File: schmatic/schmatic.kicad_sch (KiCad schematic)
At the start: 8 parts, among them J1 RFIO-RC522, J2 RTC, U1 LCD-016N002L

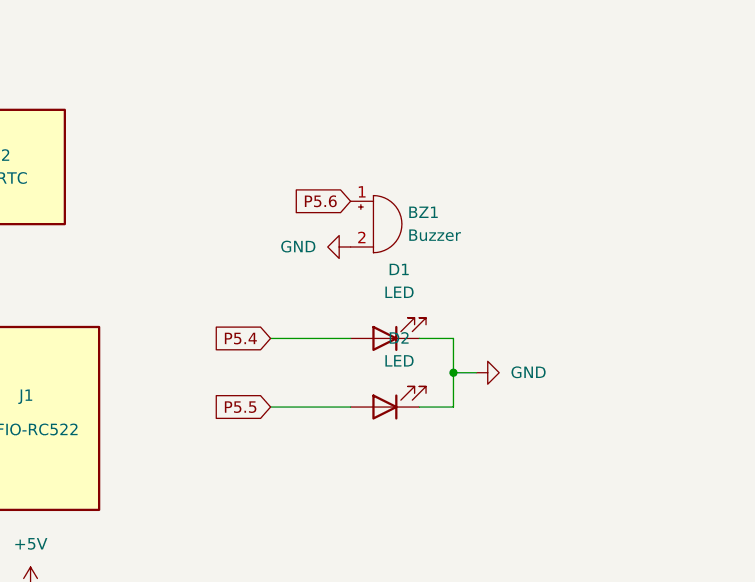
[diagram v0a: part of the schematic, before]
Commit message: fixed schmatic mistakes
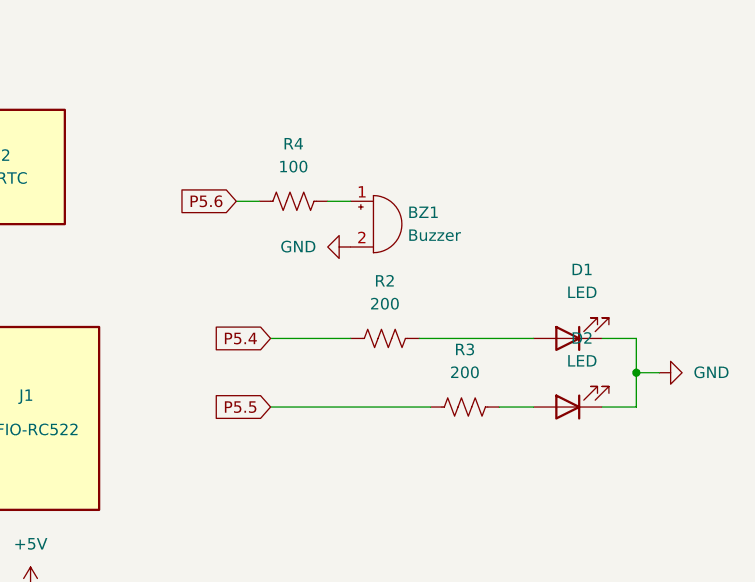
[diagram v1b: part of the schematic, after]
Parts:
- added R2, R3: 200, symbol Device:R_US
- added R4: 100, symbol Device:R_US
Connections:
- net P5.4: now also R2.1; no longer D1.2 (A)
- net P5.5: now also R3.2; no longer D2.2 (A)
- net P5.6: now also R4.2; no longer BZ1.1 (+)
- new net: D1.2 (A), R2.2
- new net: D2.2 (A), R3.1
- new net: BZ1.1 (+), R4.1
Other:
- moved on the sheet: D1, D2
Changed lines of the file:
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@@
   (junction (at 134.62 101.6) (diameter 0) (color 0 0 0 0)
   )
-  (junction (at 181.61 73.66) (diameter 0) (color 0 0 0 0)
+  (junction (at 201.93 73.66) (diameter 0) (color 0 0 0 0)
   )
   (junction (at 134.62 149.86) (diameter 0) (color 0 0 0 0)
@@
     (stroke (width 0) (type default))
   )
+  (wire (pts (xy 157.48 54.61) (xy 160.02 54.61))
+    (stroke (width 0) (type default))
+  )
   (wire (pts (xy 107.95 48.26) (xy 107.95 40.64))
     (stroke (width 0) (type default))
@@
     (stroke (width 0) (type default))
   )
-  (wire (pts (xy 181.61 69.85) (xy 181.61 73.66))
+  (wire (pts (xy 201.93 69.85) (xy 201.93 73.66))
     (stroke (width 0) (type default))
   )
@@
     (stroke (width 0) (type default))
   )
-  (wire (pts (xy 161.29 77.47) (xy 170.18 77.47))
-    (stroke (width 0) (type default))
-  )
   (wire (pts (xy 116.84 82.55) (xy 110.49 82.55))
     (stroke (width 0) (type default))
@@
     (stroke (width 0) (type default))
   )
+  (wire (pts (xy 167.64 54.61) (xy 170.18 54.61))
+    (stroke (width 0) (type default))
+  )
   (wire (pts (xy 144.78 121.92) (xy 156.21 121.92))
     (stroke (width 0) (type default))
@@
     (stroke (width 0) (type default))
   )
-  (wire (pts (xy 177.8 69.85) (xy 181.61 69.85))
+  (wire (pts (xy 198.12 69.85) (xy 201.93 69.85))
+    (stroke (width 0) (type default))
+  )
+  (wire (pts (xy 161.29 77.47) (xy 179.07 77.47))
     (stroke (width 0) (type default))
   )
@@
     (stroke (width 0) (type default))
   )
-  (wire (pts (xy 181.61 73.66) (xy 184.15 73.66))
+  (wire (pts (xy 201.93 73.66) (xy 204.47 73.66))
     (stroke (width 0) (type default))
   )
@@
     (stroke (width 0) (type default))
   )
+  (wire (pts (xy 177.8 69.85) (xy 190.5 69.85))
+    (stroke (width 0) (type default))
+  )
   (wire (pts (xy 111.76 80.01) (xy 116.84 80.01))
     (stroke (width 0) (type default))
@@
     (stroke (width 0) (type default))
   )
-  (wire (pts (xy 177.8 77.47) (xy 181.61 77.47))
+  (wire (pts (xy 198.12 77.47) (xy 201.93 77.47))
     (stroke (width 0) (type default))
   )
@@
     (stroke (width 0) (type default))
   )
+  (wire (pts (xy 110.49 85.09) (xy 116.84 85.09))
+    (stroke (width 0) (type default))
+  )
+  (wire (pts (xy 110.49 69.85) (xy 110.49 72.39))
+    (stroke (width 0) (type default))
+  )
+  (wire (pts (xy 111.76 53.34) (xy 111.76 54.61))
+    (stroke (width 0) (type default))
+  )
+  (wire (pts (xy 181.61 101.6) (xy 156.21 101.6))
+    (stroke (width 0) (type default))
+  )
+  (wire (pts (xy 201.93 77.47) (xy 201.93 73.66))
+    (stroke (width 0) (type default))
+  )
+  (wire (pts (xy 107.95 66.04) (xy 111.76 66.04))
+    (stroke (width 0) (type default))
+  )
+  (wire (pts (xy 107.95 69.85) (xy 110.49 69.85))
+    (stroke (width 0) (type default))
+  )
+  (wire (pts (xy 107.95 73.66) (xy 111.76 73.66))
+    (stroke (width 0) (type default))
+  )
+  (wire (pts (xy 186.69 77.47) (xy 190.5 77.47))
+    (stroke (width 0) (type default))
+  )
+  (wire (pts (xy 110.49 82.55) (xy 110.49 85.09))
+    (stroke (width 0) (type default))
+  )
   (wire (pts (xy 161.29 69.85) (xy 170.18 69.85))
     (stroke (width 0) (type default))
   )
-  (wire (pts (xy 110.49 85.09) (xy 116.84 85.09))
-    (stroke (width 0) (type default))
-  )
-  (wire (pts (xy 110.49 69.85) (xy 110.49 72.39))
-    (stroke (width 0) (type default))
-  )
-  (wire (pts (xy 111.76 53.34) (xy 111.76 54.61))
-    (stroke (width 0) (type default))
-  )
-  (wire (pts (xy 181.61 101.6) (xy 156.21 101.6))
-    (stroke (width 0) (type default))
-  )
-  (wire (pts (xy 181.61 77.47) (xy 181.61 73.66))
-    (stroke (width 0) (type default))
-  )
-  (wire (pts (xy 107.95 66.04) (xy 111.76 66.04))
-    (stroke (width 0) (type default))
-  )
-  (wire (pts (xy 107.95 69.85) (xy 110.49 69.85))
-    (stroke (width 0) (type default))
-  )
-  (wire (pts (xy 107.95 73.66) (xy 111.76 73.66))
-    (stroke (width 0) (type default))
-  )
-  (wire (pts (xy 110.49 82.55) (xy 110.49 85.09))
-    (stroke (width 0) (type default))
-  )
   (wire (pts (xy 116.84 48.26) (xy 107.95 48.26))
     (stroke (width 0) (type default))
@@
     )
   )
-  (global_label "P5.6" (shape input) (at 170.18 54.61 180) (fields_autoplaced)
-    (effects (font (size 1.27 1.27)) (justify right))
-    (property "Intersheetrefs" "${INTERSHEET_REFS}" (at 162.901 54.61 0)
+  (global_label "P5.6" (shape input) (at 157.48 54.61 180) (fields_autoplaced)
+    (effects (font (size 1.27 1.27)) (justify right))
+    (property "Intersheetrefs" "${INTERSHEET_REFS}" (at 150.201 54.61 0)
       (effects (font (size 1.27 1.27)) (justify right) hide)
     )
@@
     )
   )
-  (symbol (lib_id "Device:LED") (at 173.99 77.47 180) (unit 1)
-    (in_bom yes) (on_board yes) (dnp no) (fields_autoplaced)
-    (property "Reference" "D2" (at 175.5775 69.85 0)
-      (effects (font (size 1.27 1.27)))
-    )
-    (property "Value" "LED" (at 175.5775 72.39 0)
-      (effects (font (size 1.27 1.27)))
-    )
-    (property "Footprint" "" (at 173.99 77.47 0)
-      (effects (font (size 1.27 1.27)) hide)
-    )
-    (property "Datasheet" "~" (at 173.99 77.47 0)
+  (symbol (lib_id "Device:R_US") (at 173.99 69.85 90) (unit 1)
+    (in_bom yes) (on_board yes) (dnp no) (fields_autoplaced)
+    (property "Reference" "R2" (at 173.99 63.5 90)
+      (effects (font (size 1.27 1.27)))
+    )
+    (property "Value" "200" (at 173.99 66.04 90)
+      (effects (font (size 1.27 1.27)))
+    )
+    (property "Footprint" "" (at 174.244 68.834 90)
+      (effects (font (size 1.27 1.27)) hide)
+    )
+    (property "Datasheet" "~" (at 173.99 69.85 0)
+      (effects (font (size 1.27 1.27)) hide)
+    )
+    (pin "1")
+    (pin "2")
+    (instances
+      (project "schmatic"
+        (path "/4d91ea9c-4d21-4759-83b5-41660ef12129"
+          (reference "R2") (unit 1)
+        )
+      )
+    )
+  )
+  (symbol (lib_id "Device:LED") (at 194.31 77.47 180) (unit 1)
+    (in_bom yes) (on_board yes) (dnp no) (fields_autoplaced)
+    (property "Reference" "D2" (at 195.8975 69.85 0)
+      (effects (font (size 1.27 1.27)))
+    )
+    (property "Value" "LED" (at 195.8975 72.39 0)
+      (effects (font (size 1.27 1.27)))
+    )
+    (property "Footprint" "" (at 194.31 77.47 0)
+      (effects (font (size 1.27 1.27)) hide)
+    )
+    (property "Datasheet" "~" (at 194.31 77.47 0)
       (effects (font (size 1.27 1.27)) hide)
     )
@@
     )
   )
-  (symbol (lib_id "power:GND") (at 184.15 73.66 90) (unit 1)
-    (in_bom yes) (on_board yes) (dnp no) (fields_autoplaced)
-    (property "Reference" "#PWR08" (at 190.5 73.66 0)
-      (effects (font (size 1.27 1.27)) hide)
-    )
-    (property "Value" "GND" (at 187.96 73.66 90)
+  (symbol (lib_id "Device:R_US") (at 163.83 54.61 270) (unit 1)
+    (in_bom yes) (on_board yes) (dnp no) (fields_autoplaced)
+    (property "Reference" "R4" (at 163.83 48.26 90)
+      (effects (font (size 1.27 1.27)))
+    )
+    (property "Value" "100" (at 163.83 50.8 90)
+      (effects (font (size 1.27 1.27)))
+    )
+    (property "Footprint" "" (at 163.576 55.626 90)
+      (effects (font (size 1.27 1.27)) hide)
+    )
+    (property "Datasheet" "~" (at 163.83 54.61 0)
+      (effects (font (size 1.27 1.27)) hide)
+    )
+    (pin "1")
+    (pin "2")
+    (instances
+      (project "schmatic"
+        (path "/4d91ea9c-4d21-4759-83b5-41660ef12129"
+          (reference "R4") (unit 1)
+        )
+      )
+    )
+  )
+  (symbol (lib_id "Device:R_US") (at 182.88 77.47 270) (unit 1)
+    (in_bom yes) (on_board yes) (dnp no) (fields_autoplaced)
+    (property "Reference" "R3" (at 182.88 71.12 90)
+      (effects (font (size 1.27 1.27)))
+    )
+    (property "Value" "200" (at 182.88 73.66 90)
+      (effects (font (size 1.27 1.27)))
+    )
+    (property "Footprint" "" (at 182.626 78.486 90)
+      (effects (font (size 1.27 1.27)) hide)
+    )
+    (property "Datasheet" "~" (at 182.88 77.47 0)
+      (effects (font (size 1.27 1.27)) hide)
+    )
+    (pin "2")
+    (pin "1")
+    (instances
+      (project "schmatic"
+        (path "/4d91ea9c-4d21-4759-83b5-41660ef12129"
+          (reference "R3") (unit 1)
+        )
+      )
+    )
+  )
+  (symbol (lib_id "power:GND") (at 204.47 73.66 90) (unit 1)
+    (in_bom yes) (on_board yes) (dnp no) (fields_autoplaced)
+    (property "Reference" "#PWR08" (at 210.82 73.66 0)
+      (effects (font (size 1.27 1.27)) hide)
+    )
+    (property "Value" "GND" (at 208.28 73.66 90)
       (effects (font (size 1.27 1.27)) (justify right))
     )
-    (property "Footprint" "" (at 184.15 73.66 0)
-      (effects (font (size 1.27 1.27)) hide)
-    )
-    (property "Datasheet" "" (at 184.15 73.66 0)
+    (property "Footprint" "" (at 204.47 73.66 0)
+      (effects (font (size 1.27 1.27)) hide)
+    )
+    (property "Datasheet" "" (at 204.47 73.66 0)
       (effects (font (size 1.27 1.27)) hide)
     )
@@
     )
   )
-  (symbol (lib_id "Device:LED") (at 173.99 69.85 180) (unit 1)
-    (in_bom yes) (on_board yes) (dnp no) (fields_autoplaced)
-    (property "Reference" "D1" (at 175.5775 62.23 0)
-      (effects (font (size 1.27 1.27)))
-    )
-    (property "Value" "LED" (at 175.5775 64.77 0)
-      (effects (font (size 1.27 1.27)))
-    )
-    (property "Footprint" "" (at 173.99 69.85 0)
-      (effects (font (size 1.27 1.27)) hide)
-    )
-    (property "Datasheet" "~" (at 173.99 69.85 0)
-      (effects (font (size 1.27 1.27)) hide)
-    )
+  (symbol (lib_id "Device:LED") (at 194.31 69.85 180) (unit 1)
+    (in_bom yes) (on_board yes) (dnp no) (fields_autoplaced)
+    (property "Reference" "D1" (at 195.8975 62.23 0)
+      (effects (font (size 1.27 1.27)))
+    )
+    (property "Value" "LED" (at 195.8975 64.77 0)
+      (effects (font (size 1.27 1.27)))
+    )
+    (property "Footprint" "" (at 194.31 69.85 0)
+      (effects (font (size 1.27 1.27)) hide)
+    )
+    (property "Datasheet" "~" (at 194.31 69.85 0)
+      (effects (font (size 1.27 1.27)) hide)
+    )

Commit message: updated schmatic
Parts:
- removed R4: 100, symbol Device:R_US
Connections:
- net +3.3V: no longer J2.2 (VCC)
- net +5V: now also J2.2 (VCC)
- net P5.6: now also BZ1.1 (+)
- net P3.0: no longer names the net of J1.5 (RQ)
- net P5.4 renamed P2.4
- net P5.5 renamed P2.3
- no-connect marks 1 -> 2
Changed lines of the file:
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@@
   )
   (no_connect (at 114.3 55.88))
+  (no_connect (at 116.84 80.01))
   (wire (pts (xy 116.84 129.54) (xy 124.46 129.54))
     (stroke (width 0) (type default))
@@
     (stroke (width 0) (type default))
   )
-  (wire (pts (xy 157.48 54.61) (xy 160.02 54.61))
+  (wire (pts (xy 166.37 54.61) (xy 170.18 54.61))
     (stroke (width 0) (type default))
   )
@@
     (stroke (width 0) (type default))
   )
+  (wire (pts (xy 166.37 59.69) (xy 170.18 59.69))
+    (stroke (width 0) (type default))
+  )
   (wire (pts (xy 115.57 110.49) (xy 120.65 110.49))
     (stroke (width 0) (type default))
@@
     (stroke (width 0) (type default))
   )
-  (wire (pts (xy 107.95 81.28) (xy 111.76 81.28))
-    (stroke (width 0) (type default))
-  )
   (wire (pts (xy 116.84 82.55) (xy 110.49 82.55))
     (stroke (width 0) (type default))
@@
     (stroke (width 0) (type default))
   )
-  (wire (pts (xy 167.64 54.61) (xy 170.18 54.61))
-    (stroke (width 0) (type default))
-  )
   (wire (pts (xy 144.78 121.92) (xy 156.21 121.92))
     (stroke (width 0) (type default))
@@
     (stroke (width 0) (type default))
   )
-  (wire (pts (xy 111.76 80.01) (xy 116.84 80.01))
-    (stroke (width 0) (type default))
-  )
   (wire (pts (xy 105.41 101.6) (xy 134.62 101.6))
     (stroke (width 0) (type default))
@@
     (stroke (width 0) (type default))
   )
-  (wire (pts (xy 111.76 81.28) (xy 111.76 80.01))
-    (stroke (width 0) (type default))
-  )
   (wire (pts (xy 120.65 111.76) (xy 124.46 111.76))
     (stroke (width 0) (type default))
@@
     (stroke (width 0) (type default))
   )
-  (global_label "P5.5" (shape input) (at 161.29 77.47 180) (fields_autoplaced)
+  (global_label "P2.3" (shape input) (at 161.29 77.47 180) (fields_autoplaced)
     (effects (font (size 1.27 1.27)) (justify right))
     (property "Intersheetrefs" "${INTERSHEET_REFS}" (at 154.011 77.47 0)
@@
     )
   )
-  (global_label "P5.6" (shape input) (at 157.48 54.61 180) (fields_autoplaced)
-    (effects (font (size 1.27 1.27)) (justify right))
-    (property "Intersheetrefs" "${INTERSHEET_REFS}" (at 150.201 54.61 0)
+  (global_label "P5.6" (shape input) (at 166.37 54.61 180) (fields_autoplaced)
+    (effects (font (size 1.27 1.27)) (justify right))
+    (property "Intersheetrefs" "${INTERSHEET_REFS}" (at 159.091 54.61 0)
       (effects (font (size 1.27 1.27)) (justify right) hide)
     )
@@
     )
   )
-  (global_label "P5.4" (shape input) (at 161.29 69.85 180) (fields_autoplaced)
+  (global_label "P2.4" (shape input) (at 161.29 69.85 180) (fields_autoplaced)
     (effects (font (size 1.27 1.27)) (justify right))
     (property "Intersheetrefs" "${INTERSHEET_REFS}" (at 154.011 69.85 0)
@@
     (effects (font (size 1.27 1.27)) (justify right))
     (property "Intersheetrefs" "${INTERSHEET_REFS}" (at 100.671 50.8 0)
-      (effects (font (size 1.27 1.27)) (justify right) hide)
-    )
-  )
-  (global_label "P3.0" (shape input) (at 107.95 81.28 180) (fields_autoplaced)
-    (effects (font (size 1.27 1.27)) (justify right))
-    (property "Intersheetrefs" "${INTERSHEET_REFS}" (at 100.671 81.28 0)
       (effects (font (size 1.27 1.27)) (justify right) hide)
     )
@@
     )
   )
-  (symbol (lib_id "power:+3.3V") (at 107.95 40.64 0) (unit 1)
-    (in_bom yes) (on_board yes) (dnp no) (fields_autoplaced)
-    (property "Reference" "#PWR03" (at 107.95 44.45 0)
-      (effects (font (size 1.27 1.27)) hide)
-    )
-    (property "Value" "+3.3V" (at 107.95 35.56 0)
-      (effects (font (size 1.27 1.27)))
-    )
-    (property "Footprint" "" (at 107.95 40.64 0)
-      (effects (font (size 1.27 1.27)) hide)
-    )
-    (property "Datasheet" "" (at 107.95 40.64 0)
-      (effects (font (size 1.27 1.27)) hide)
-    )
-    (pin "1")
-    (instances
-      (project "schmatic"
-        (path "/4d91ea9c-4d21-4759-83b5-41660ef12129"
-          (reference "#PWR03") (unit 1)
-        )
-      )
-    )
-  )
   (symbol (lib_id "Device:R_US") (at 173.99 69.85 90) (unit 1)
     (in_bom yes) (on_board yes) (dnp no) (fields_autoplaced)
@@
     )
   )
-  (symbol (lib_id "Device:R_US") (at 163.83 54.61 270) (unit 1)
-    (in_bom yes) (on_board yes) (dnp no) (fields_autoplaced)
-    (property "Reference" "R4" (at 163.83 48.26 90)
-      (effects (font (size 1.27 1.27)))
-    )
-    (property "Value" "100" (at 163.83 50.8 90)
-      (effects (font (size 1.27 1.27)))
-    )
-    (property "Footprint" "" (at 163.576 55.626 90)
-      (effects (font (size 1.27 1.27)) hide)
-    )
-    (property "Datasheet" "~" (at 163.83 54.61 0)
-      (effects (font (size 1.27 1.27)) hide)
-    )
-    (pin "1")
-    (pin "2")
-    (instances
-      (project "schmatic"
-        (path "/4d91ea9c-4d21-4759-83b5-41660ef12129"
-          (reference "R4") (unit 1)
-        )
-      )
-    )
-  )
   (symbol (lib_id "Device:R_US") (at 182.88 77.47 270) (unit 1)
     (in_bom yes) (on_board yes) (dnp no) (fields_autoplaced)
@@
     )
   )
-  (symbol (lib_id "power:GND") (at 170.18 59.69 270) (unit 1)
-    (in_bom yes) (on_board yes) (dnp no) (fields_autoplaced)
-    (property "Reference" "#PWR07" (at 163.83 59.69 0)
-      (effects (font (size 1.27 1.27)) hide)
-    )
-    (property "Value" "GND" (at 166.37 59.69 90)
+  (symbol (lib_id "power:GND") (at 166.37 59.69 270) (unit 1)
+    (in_bom yes) (on_board yes) (dnp no) (fields_autoplaced)
+    (property "Reference" "#PWR07" (at 160.02 59.69 0)
+      (effects (font (size 1.27 1.27)) hide)
+    )
+    (property "Value" "GND" (at 162.56 59.69 90)
       (effects (font (size 1.27 1.27)) (justify right))
     )
-    (property "Footprint" "" (at 170.18 59.69 0)
-      (effects (font (size 1.27 1.27)) hide)
-    )
-    (property "Datasheet" "" (at 170.18 59.69 0)
+    (property "Footprint" "" (at 166.37 59.69 0)
+      (effects (font (size 1.27 1.27)) hide)
+    )
+    (property "Datasheet" "" (at 166.37 59.69 0)
       (effects (font (size 1.27 1.27)) hide)
     )
@@
         )
       )
+    )
+  )
+  (symbol (lib_id "power:+5V") (at 107.95 40.64 0) (unit 1)
+    (in_bom yes) (on_board yes) (dnp no) (fields_autoplaced)
+    (property "Reference" "#PWR03" (at 107.95 44.45 0)
+      (effects (font (size 1.27 1.27)) hide)
+    )
+    (property "Value" "+5V" (at 107.95 35.56 0)
+      (effects (font (size 1.27 1.27)))
+    )
+    (property "Footprint" "" (at 107.95 40.64 0)
+      (effects (font (size 1.27 1.27)) hide)
+    )
+    (property "Datasheet" "" (at 107.95 40.64 0)
+      (effects (font (size 1.27 1.27)) hide)
+    )
+    (pin "1")
+    (instances
+      (project "schmatic"
+        (path "/4d91ea9c-4d21-4759-83b5-41660ef12129"
+          (reference "#PWR03") (unit 1)
+        )
+      )

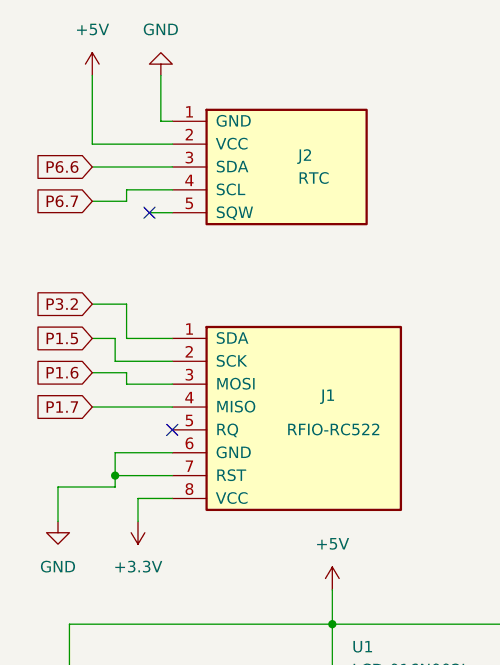
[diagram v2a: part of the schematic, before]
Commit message: flowchart updates and code cleanup
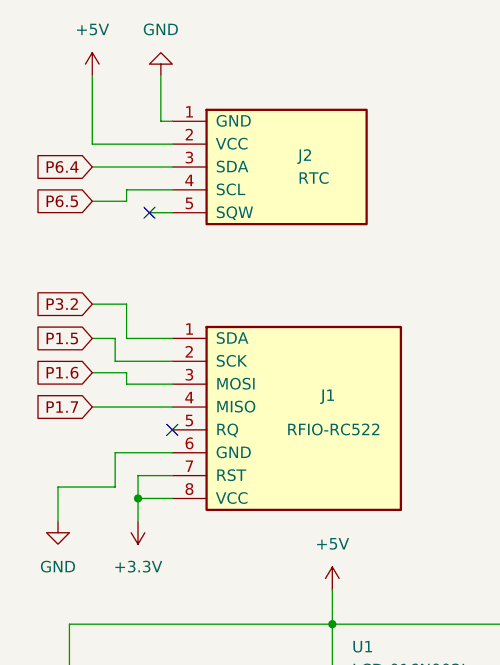
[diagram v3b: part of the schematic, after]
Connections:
- net +3.3V: now also J1.7 (RST)
- net GND: no longer J1.7 (RST)
- net P6.6 renamed P6.4
- net P6.7 renamed P6.5
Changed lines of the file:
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@@
 (kicad_sch (version 20230121) (generator eeschema)
   (paper "A")
-  (junction (at 110.49 85.09) (diameter 0) (color 0 0 0 0)
+  (junction (at 113.03 87.63) (diameter 0) (color 0 0 0 0)
   )
   (junction (at 156.21 121.92) (diameter 0) (color 0 0 0 0)
@@
     (stroke (width 0) (type default))
   )
+  (wire (pts (xy 116.84 85.09) (xy 113.03 85.09))
+    (stroke (width 0) (type default))
+  )
   (wire (pts (xy 111.76 54.61) (xy 107.95 54.61))
     (stroke (width 0) (type default))
@@
     (stroke (width 0) (type default))
   )
-  (wire (pts (xy 110.49 85.09) (xy 110.49 86.36))
+  (wire (pts (xy 110.49 82.55) (xy 110.49 86.36))
     (stroke (width 0) (type default))
   )
@@
     (stroke (width 0) (type default))
   )
+  (wire (pts (xy 113.03 85.09) (xy 113.03 87.63))
+    (stroke (width 0) (type default))
+  )
   (wire (pts (xy 134.62 149.86) (xy 156.21 149.86))
     (stroke (width 0) (type default))
@@
     (stroke (width 0) (type default))
   )
-  (wire (pts (xy 110.49 85.09) (xy 116.84 85.09))
-    (stroke (width 0) (type default))
-  )
   (wire (pts (xy 110.49 69.85) (xy 110.49 72.39))
     (stroke (width 0) (type default))
@@
     (stroke (width 0) (type default))
   )
-  (wire (pts (xy 110.49 82.55) (xy 110.49 85.09))
-    (stroke (width 0) (type default))
-  )
   (wire (pts (xy 161.29 69.85) (xy 170.18 69.85))
     (stroke (width 0) (type default))
@@
     )
   )
-  (global_label "P6.7" (shape input) (at 107.95 54.61 180) (fields_autoplaced)
+  (global_label "P6.5" (shape input) (at 107.95 54.61 180) (fields_autoplaced)
     (effects (font (size 1.27 1.27)) (justify right))
     (property "Intersheetrefs" "${INTERSHEET_REFS}" (at 100.671 54.61 0)
@@
     )
   )
-  (global_label "P6.6" (shape input) (at 107.95 50.8 180) (fields_autoplaced)
+  (global_label "P6.4" (shape input) (at 107.95 50.8 180) (fields_autoplaced)
     (effects (font (size 1.27 1.27)) (justify right))
     (property "Intersheetrefs" "${INTERSHEET_REFS}" (at 100.671 50.8 0)
